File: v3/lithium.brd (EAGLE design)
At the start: 86.4 x 54.6 mm, 60 parts, among them J1 batt, J2 battery, J3 motor, J4 AVR_ISP, Q1_R1 100k, U1 TPS61088VQFN20, U1_C22 8.2nF, U1_CBST 100nF, U1_CCOMP 680PF, U1_CCOMP2 36pF, U1_CIN 0.47uF, U1_CIN2 100nF, U1_COUT 0.47uF, U1_CVCC 1uF, U1_L1 DR73-1R0-R, U1_RCOMP 38.3K Ohms, U1_RFBB 118K Ohms, U1_RFBT 470K Ohms, U1_RLIM 102K Ohms, U1_RT 261K Ohms, U2 ATTINY84-20MU, U2_C1 22uF, U2_C2 22uF, U2_R1 10k, U2_R2 10k, U4 TPS2113APWR, U4_C3 0.1uF, U4_C4 0.1uF, U4_RPG 100K Ohms, U5 MCP73833-FCI/UN, U5_C1 1.0uF, U5_C2 1.0uF, U5_R1 1K Ohm, U6 TPS61230A, U6_CBST 10 nF, U6_CFF 10pF, U6_CIN 22uF, U6_COUT 22uF, U6_RFBB 100K Ohms, U6_RFBT 316K Ohms

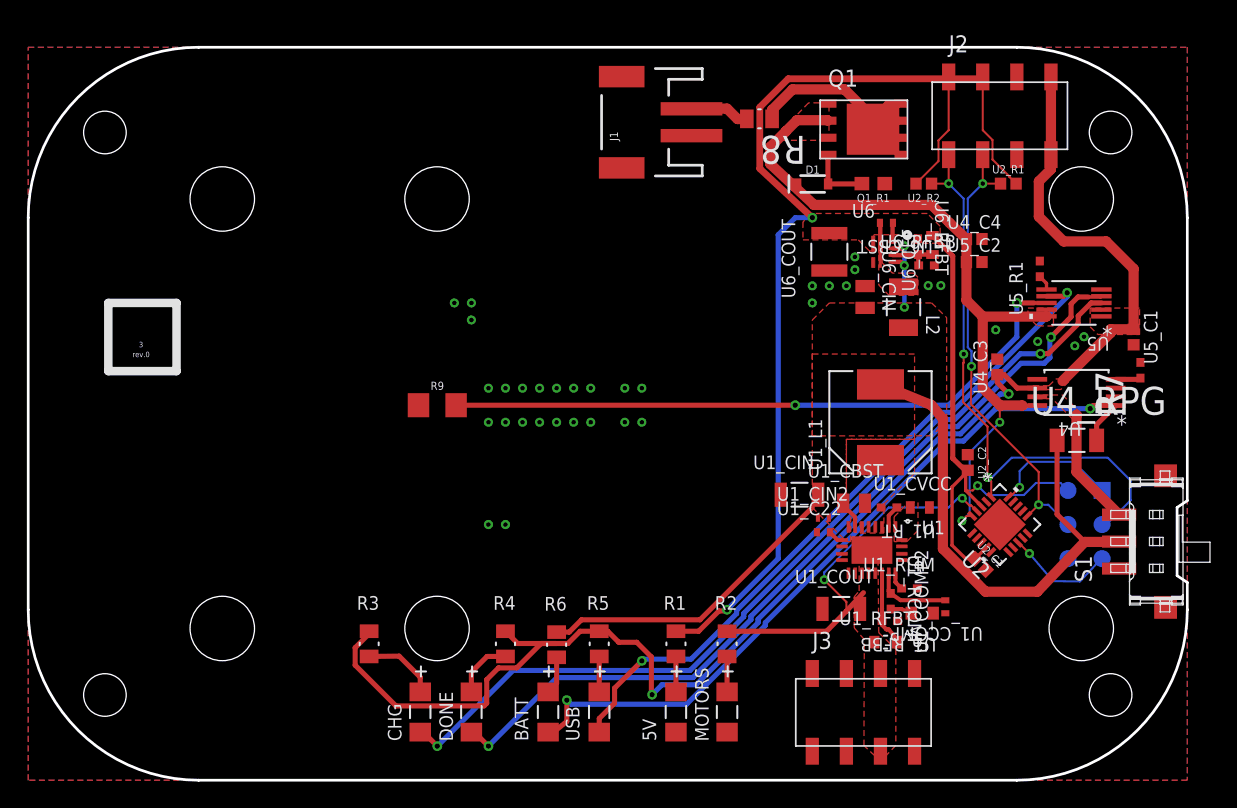
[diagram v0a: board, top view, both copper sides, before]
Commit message: Major layout completion.
Still need some via stitching of gnd and silkscreen.
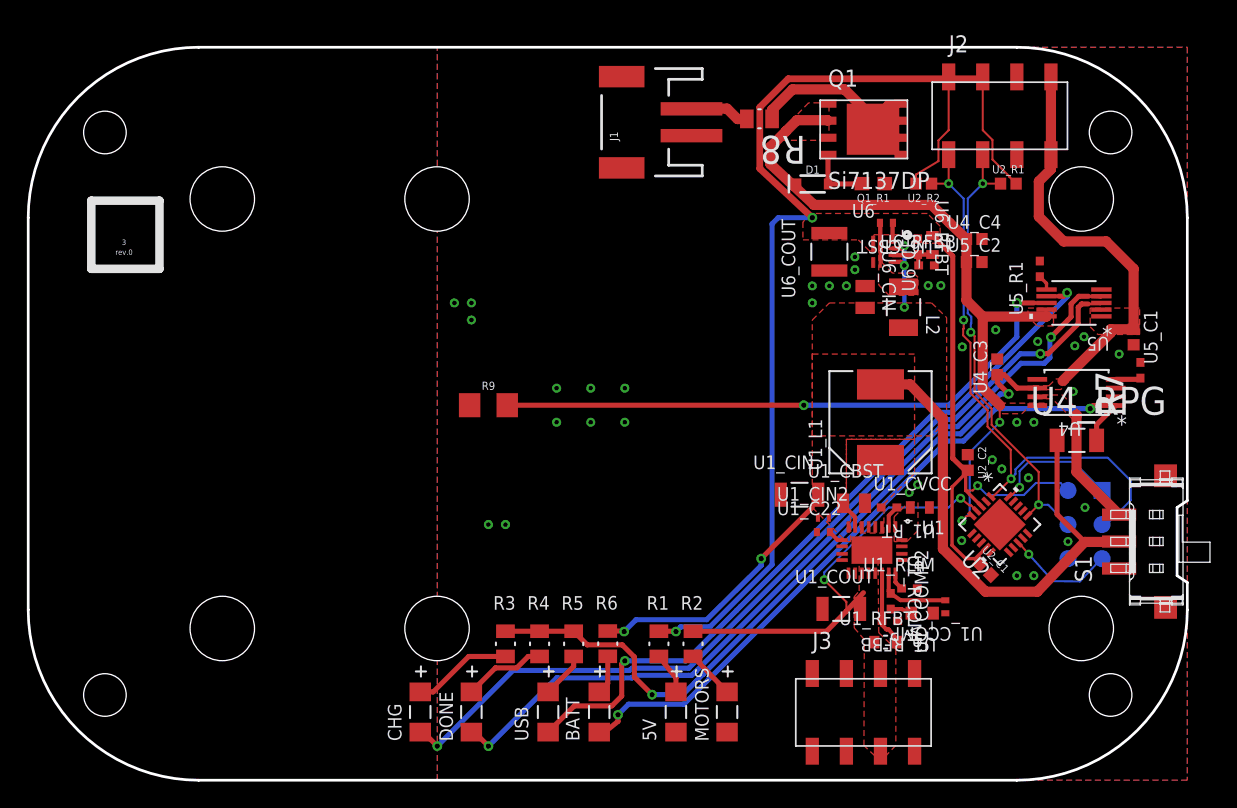
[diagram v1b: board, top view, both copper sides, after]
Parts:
- Q1: value (none) -> Si7137DP
- moved R3 10.2 mm to (36.8, 11.4)
- moved 3 7.73 mm to (11.1, 39.4)
- moved R6 3.81 mm to (44.5, 11.4)
- moved R9 3.81 mm to (35.6, 29.2)
- moved BATT 3.81 mm to (43.8, 6.35)
- moved USB 3.81 mm to (40.0, 6.35)
- moved R2 2.54 mm to (50.8, 11.4)
- moved R4 2.54 mm to (39.4, 11.4)
- moved R5 1.91 mm to (41.9, 11.4)
- moved R1 1.27 mm to (48.3, 11.4)
- moved U2_C1 0.54 mm to (72.6, 17.0)
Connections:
- net VBAT_MON renamed VBAT_CON
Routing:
- net VUSB: track 109.7 -> 86.0 mm
- net U4_STAT: track 56.8 -> 52.0 mm
- net U5_NPG: track 51.6 -> 55.6 mm
- net U5_THERM: track 48.6 -> 44.8 mm
- net VCC: track 69.0 -> 65.8 mm, vias 3 -> 5
- net SYS_5V: track 122.2 -> 125.0 mm
- net VBAT: track 55.2 -> 52.5 mm
- net MOT_6V: track 29.0 -> 31.5 mm
- net LA_CHG: track 5.55 -> 7.44 mm
- net LA_DONE: track 4.50 -> 6.17 mm
- net LA_6: track 2.64 -> 3.66 mm
- net LA_USB: track 2.64 -> 3.43 mm

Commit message: Okay, I think this fixed it.
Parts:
- U2_C1: value 22uF -> 10nF; device 32bits:0402 -> Yageo_By_element14_Batch_1:CAPC1005X55N
- U2_C2: value 22uF -> 2.2uF; device 32bits:0402 -> AVX_By_element14_Batch_1:CAPC1005X60N
- moved U2_C1 7.76 mm to (71.4, 24.6), turned to 225 degrees
- moved U2_C2 7.63 mm to (72.3, 17.4), turned to 135 degrees
- moved U1_CIN 2.54 mm to (58.7, 25.1)
- moved U1_CIN2 2.41 mm to (59.5, 23.0)
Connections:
- net GND: now also U2_C1.1; no longer U2_C1.2
- net SYS_5V: now also U2_C1.2; no longer U2_C1.1
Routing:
- net SYS_5V: track 125.0 -> 124.5 mm

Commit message: Release candidate.
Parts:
- moved 3 3.81 mm to (11.1, 35.6)
- moved U1_CIN2 2.54 mm to (59.5, 25.6)
- moved U1_CIN 2.49 mm to (58.8, 27.6)
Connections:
- net LOCAL_VBAT renamed VBAT_JST
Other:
- board text added: "+5IN"
- board text added: "5V"
- board text added: "6V"
- board text added: "SCK"
- board text added: "SDA"

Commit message: Seed order 170325111000
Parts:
- moved U1_CCOMP 0.78 mm to (67.9, 12.9), turned to 90 degrees
- moved U4_C3 0.69 mm to (74.1, 31.8), turned to 45 degrees
- moved U6_COUT 0.66 mm to (60.3, 40.7)
- moved U6_CFF 0.57 mm to (68.5, 41.7)
- moved U6_CIN 0.48 mm to (63.1, 37.2)
- moved U1_CVCC 0.28 mm to (67.7, 21.3)
- moved R7 0.25 mm to (84.1, 31.6)
- moved U1_C22 0.25 mm to (60.6, 19.5), turned to 45 degrees
- moved U1_CCOMP2 0.20 mm to (69.4, 14.2)
- moved U1_CIN 0.18 mm to (58.9, 27.4)
- moved U6_CBST 0.15 mm to (65.2, 42.6)
- moved U1_RLIM 0.13 mm to (66.9, 15.7)
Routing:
- net SYS_5V: track 124.5 -> 130.6 mm
- net N$1: track 1.60 -> 2.46 mm

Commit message: Some small, post-rev0 tweaks.
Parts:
- R1, R3, R5: value 15 Ohm -> 150 Ohm; device Vishay_By_element14_Batch_1:RESC2013X65N -> Panasonic_By_element14_Batch_1:RESC2013X65N
- R2: value 15 Ohm -> 200 Ohm; device Vishay_By_element14_Batch_1:RESC2013X65N -> Panasonic_By_element14_Batch_1:RESC2013X65N
- R4, R6: value 15 Ohm -> 100 Ohm; device Vishay_By_element14_Batch_1:RESC2013X65N -> Panasonic_By_element14_Batch_1:RESC2013X65N
